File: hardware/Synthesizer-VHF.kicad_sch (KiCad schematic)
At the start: 106 parts, among them J1 Screw_Terminal_01x02, J10 REF_OUT, J12 UPDI, J2 Scope, J4 USB-C 2.0 16P, J5 REF_IN, J6 Scope, J7 RFOUTA, J9 RFOUTB, U1 LM7805A, U11 SN74LVC1GU04DBVR, U2 FT231XQ, U3 ATtiny1616-M, U4 ADF4351, U5 USBLC6-2SC6, U6 LP5907MFX-3.3, U8 LP5907MFX-3.3, X1 IQXT-220-2 10MHz

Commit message: diecast-2x2: ADF4002 locks the VCTCXO to REF_IN
Add ADF4002BCPZ (LCSC C207536). REFIN is external REF_IN through the existing attenuator, AC-coupled. RFIN is an AC-coupled VCTCXO sample. SPI CLK and DATA are shared with the ADF4351; LE is PA7 and MUXOUT is PA5. Passive loop filter is 1.5 nF, 2.2 M, 10 nF for about 20 Hz at the lowest charge-pump current. PA6 holds Vc through 100 k.

Co-authored-by: Jeffrey Millar <wa1hco@users.noreply.github.com>
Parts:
- added C55: 1.5n, Capacitor_SMD:C_0603_1608Metric, symbol Device:C
- added C56: 10n, Capacitor_SMD:C_0603_1608Metric, symbol Device:C
- added C57, C58, C60, C61: 100n, Synthesizer:Cap_0402, symbol Device:C
- added C59: 100p, Synthesizer:Cap_0402, symbol Device:C
- added R34: 2.2M, Resistor_SMD:R_0603_1608Metric, symbol Device:R_Small_US
- added R35: 5K1, Synthesizer:Res_0402, symbol Device:R_Small_US
- added R36: 100k, Synthesizer:Res_0402, symbol Device:R_Small_US
- added U12: ADF4002BCPZ, Package_DFN_QFN:QFN-20-1EP_4x4mm_P0.5mm_EP2.5x2.5mm, symbol Synthesizer:ADF4002BCPZ
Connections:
- net CLK: now also U12.12 (CLK)
- net DATA: now also U12.13 (DATA)
- net GND: now also C55.2, C56.2, C59.2, C60.2, C61.2, R35.2, U12.1 (CPGND), U12.10 (DGND), U12.2 (AGND), U12.21 (EP), U12.3 (AGND), U12.9 (DGND)
- net REF_IN: now also C58.1
- net VC: now also C56.1, R34.2, R36.2
- net VDD: now also C61.1, U12.11 (CE), U12.16 (DVDD), U12.17 (DVDD)
- net VRF: now also C60.1, U12.18 (VP), U12.6 (AVDD), U12.7 (AVDD)
- net XO: now also C57.1
- net MUX4002: now reaches U3.6 (PA5)
- net MUX4002: now also U12.15 (MUXOUT)
- net DAC_HOLD: now reaches U3.7 (PA6)
- net DAC_HOLD: now also R36.1
- net LE4002: now reaches U3.8 (PA7)
- net LE4002: now also U12.14 (LE)
- new net CP: C55.1, R34.1, U12.20 (CP)
- new net REFIN4: C58.2, U12.8 (REFIN)
- new net RFINA: C57.2, U12.5 (RFINA)
- new net RFINB: C59.1, U12.4 (RFINB)
- new net RSET: R35.1, U12.19 (RSET)
- no-connect marks 12 -> 9
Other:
- note added: "ADF4002 loop filter, about 20 Hz, 50 deg phase margin. Kvco = 10 MHz * 20 ppm / 2 V = 100 Hz/V. IQXT-220-2 pulling is +/-10 to +/-15 ppm over Vc = 1.5 V +/- 1 V, so Kv is about 100-150 Hz/V. Designed at 100 Hz/V. PFD = 10 kHz with R = N = 1000 (10 MHz / 10 kHz). Lowest CP current: CPI=000, RSET=5.1k, Icp=0.625 mA. T1=(sec phi - tan phi)/wc = 2.90 ms, T2=1/(wc^2*T1)=21.9 ms. C1=1.5 nF C0G (CP to G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"

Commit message: diecast-2x2: merge scope headers into one 1x5
Replace J2 and J6 with a single 1x5 header: LD, MUX, DBG1, DBG2, GND (LCSC C124379). DBG1 and DBG2 are header pads only, because PB4 and PB5 are reserved for the lock LEDs.

Co-authored-by: Jeffrey Millar <wa1hco@users.noreply.github.com>
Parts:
- removed J2, J6: Scope, Connector_PinHeader_2.54mm:PinHeader_1x03_P2.54mm_Vertical, symbol Connector:Conn_01x03_Pin
- added J2: Scope, Connector_PinHeader_2.54mm:PinHeader_1x05_P2.54mm_Vertical, symbol Synthesizer:Conn_01x05_Pin
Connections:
- net GND: now also J2.5 (Pin_5)
- net LD: now also J2.1 (Pin_1); no longer U4.25 (LD)
- net MUX: now also J2.2 (Pin_2); no longer U4.30 (MUXOUT)
- new net DBG1: J2.3 (Pin_3)
- new net DBG2: J2.4 (Pin_4)
- no-connect marks 9 -> 11

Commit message: diecast-2x2: four reverse-mount status LEDs
Replace the 0402 status LEDs with Kingbright KPTL-3216 reverse-mount parts that shine through the board. PWR and COMM are green C598390; REF LOCK (PB4) and SYNTH LOCK (PB5) are red C598393. COMM is FT231X CBUS2, to be programmed as TX&RXLED#.

Co-authored-by: Jeffrey Millar <wa1hco@users.noreply.github.com>
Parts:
- removed D4, D5: Yellow, LED_SMD:LED_0402_1005Metric, symbol Device:LED
- removed D7: PA2, LED_SMD:LED_0402_1005Metric, symbol Device:LED
- removed D8: PA3, LED_SMD:LED_0402_1005Metric, symbol Device:LED
- removed R10, R17, R19, R8: 1K, Synthesizer:Res_0402, symbol Device:R_US
- added D11: PWR, Synthesizer:LED_KPTL-3216_ReverseMount, symbol Device:LED
- added D12: REF LOCK, Synthesizer:LED_KPTL-3216_ReverseMount, symbol Device:LED
- added D13: SYNTH LOCK, Synthesizer:LED_KPTL-3216_ReverseMount, symbol Device:LED
- added D14: COMM, Synthesizer:LED_KPTL-3216_ReverseMount, symbol Device:LED
- added R37, R38, R39, R40: 1k, Synthesizer:Res_0402, symbol Device:R_Small_US
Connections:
- net GND: now also D11.1 (K), D12.1 (K), D13.1 (K)
- net VDD: now also D14.2 (A), R37.1
- net REF_LOCK: now reaches U3.10 (PB4)
- net REF_LOCK: now also R38.1
- net SYNTH_LOCK: now reaches U3.9 (PB5)
- net SYNTH_LOCK: now also R39.1
- net RXLED/: no longer names the net of U2.14 (CBUS1)
- net TXLED/ renamed CBUS_ACT
- net CBUS_ACT: now also R40.2
- new net COMM_K: D14.1 (K), R40.1
- new net PWR_A: D11.2 (A), R37.2
- new net REFLED: D12.2 (A), R38.2
- new net SYNLED: D13.2 (A), R39.2
- no-connect marks 11 -> 12
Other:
- note added: "CBUS2 (pin 7) is the COMM LED, active low. Program it as TX&RXLED#."
- note added: "PCB: 1.5 mm hole under each LED with GND via ring (waveguide below cutoff). Reverse-mount Kingbright KPTL-3216. Light exits the bottom face. PWR and COMM are green KPTL-3216CGCK-01 (C598390). REF LOCK and SYNTH LOCK are red KPTL-3216SURCK-01 (C598393). Blue KPTL-3216QBC-D-01 is on LCSC but Vf is 3.3 V, so it is not used on this 3.3 V rail."
- note removed: "CBUS signals use defaults"

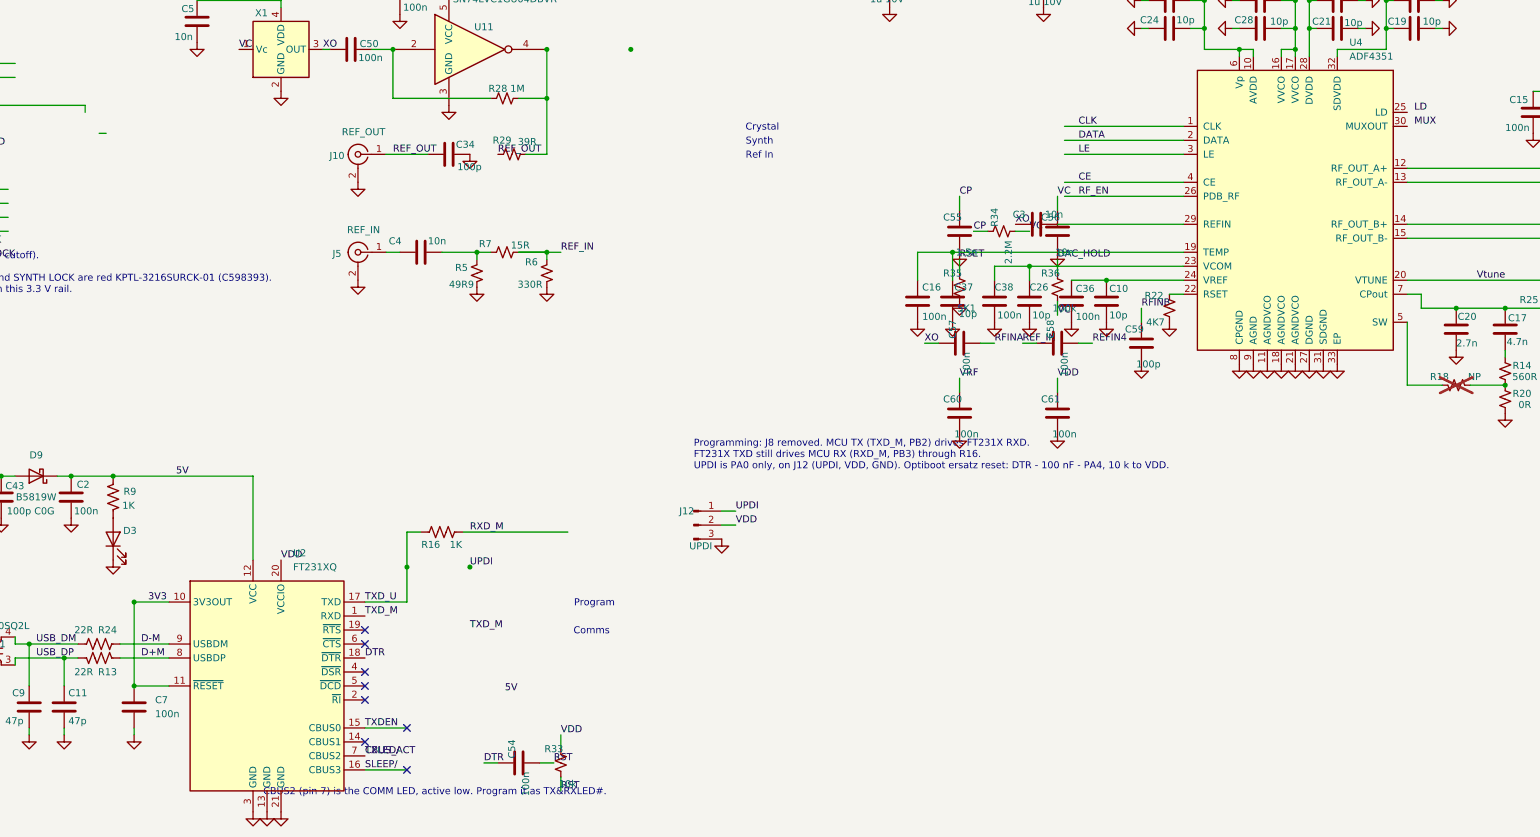
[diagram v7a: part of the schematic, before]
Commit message: diecast-2x2: make the schematic load in KiCad 10 ERC
Escape multiline notes, fix symbol property hide flags, drop dangling labels left by the removed headers, and put LD and MUX back on the ADF4351 pins.

Co-authored-by: Jeffrey Millar <wa1hco@users.noreply.github.com>
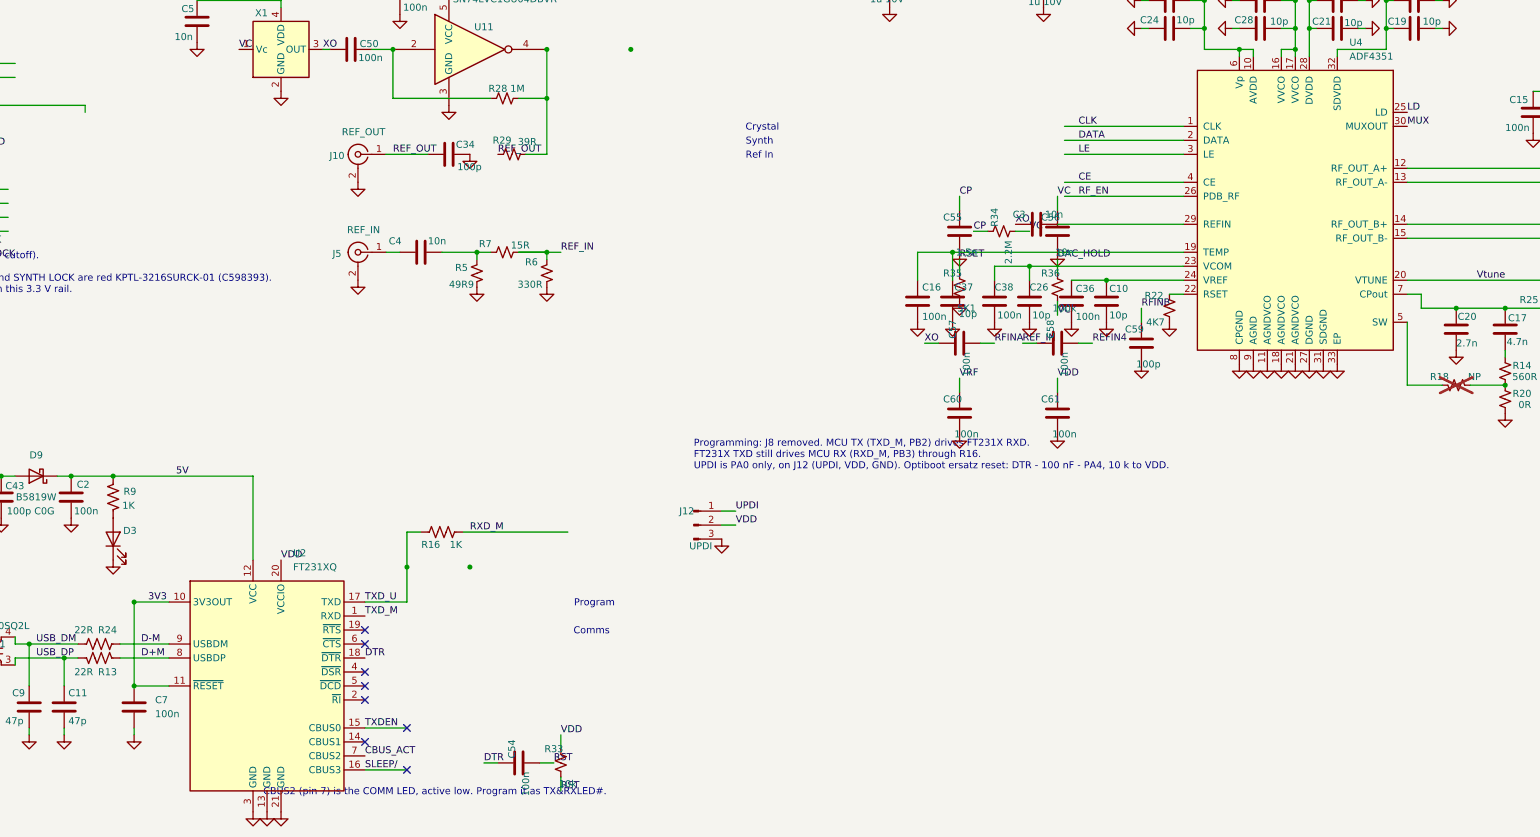
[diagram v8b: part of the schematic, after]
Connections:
- net LD: now also U4.25 (LD)
- net MUX: now also U4.30 (MUXOUT)
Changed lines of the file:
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@@
 		)
 	)
-	(wire
-		(pts
-			(xy 93.98 139.7) (xy 92.71 139.7)
-		)
-		(stroke
-			(width 0)
-			(type default)
-		)
-	)
-	(wire
+		(wire
 		(pts
 			(xy 374.65 139.7) (xy 374.65 156.21)
@@
 		)
 	)
-	(label "TXD_M"
-		(at 160.02 229.87 0)
-		(effects
-			(font
-				(size 1.27 1.27)
-			)
-			(justify left bottom)
-		)
-	)
-	(label "LD"
-		(at 331.47 135.89 0)
-		(effects
-			(font
-				(size 1.27 1.27)
-			)
-			(justify left bottom)
-		)
-	)
-	(label "5V_USB"
+			(label "5V_USB"
 		(at 67.31 201.93 0)
 		(effects
@@
 		)
 	)
-	(label "5V"
-		(at 166.37 241.3 0)
-		(effects
-			(font
-				(size 1.27 1.27)
-			)
-			(justify left bottom)
-		)
-	)
-	(label "RF_EN"
+		(label "RF_EN"
 		(at 270.51 151.13 0)
 		(effects
@@
 		)
 	)
-	(label "UPDI"
-		(at 160.02 218.44 0)
-		(effects
-			(font
-				(size 1.27 1.27)
-			)
-			(justify left bottom)
-		)
-	)
-	(label "TXLED{slash}"
-		(at 140.97 252.73 0)
-		(effects
-			(font
-				(size 1.27 1.27)
-			)
-			(justify left bottom)
-		)
-	)
-	(label "5V"
+			(label "5V"
 		(at 106.68 201.93 0)
 		(effects
@@
 		)
 	)
-	(label "MUX"
-		(at 331.47 138.43 0)
-		(effects
-			(font
-				(size 1.27 1.27)
-			)
-			(justify left bottom)
-		)
-	)
-	(symbol
+		(symbol
 		(lib_id "Device:C")
 		(at 236.22 43.18 0)
@@
 		)
 	)
-	(text "Digital 3.3 V (VDD): ATtiny, FT231X VCCIO, ADF4002 DVDD, VCTCXO, REF buffer.
-Fed from the VRF LP5907 through FB2. VVCO is its own LP5907. ADF4351 AVDD/Vp are on VRF."
+	(text "Digital 3.3 V (VDD): ATtiny, FT231X VCCIO, ADF4002 DVDD, VCTCXO, REF buffer.\nFed from the VRF LP5907 through FB2. VVCO is its own LP5907. ADF4351 AVDD/Vp are on VRF."
 		(exclude_from_sim no)
 		(at 292.1 22.86 0)
@@
 		)
 	)
-	(text "Programming: J8 removed. MCU TX (TXD_M, PB2) drives FT231X RXD.
-FT231X TXD still drives MCU RX (RXD_M, PB3) through R16.
-UPDI is PA0 only, on J12 (UPDI, VDD, GND). Optiboot ersatz reset: DTR - 100 nF - PA4, 10 k to VDD."
+	(text "Programming: J8 removed. MCU TX (TXD_M, PB2) drives FT231X RXD.\nFT231X TXD still drives MCU RX (RXD_M, PB3) through R16.\nUPDI is PA0 only, on J12 (UPDI, VDD, GND). Optiboot ersatz reset: DTR - 100 nF - PA4, 10 k to VDD."
 		(exclude_from_sim no)
 		(at 200.66 198.12 0)
@@
 		)
 	)
-	(text "REF_OUT: after U11, 39 ohm series and 100 pF to GND. RC edge softener, not a sine filter.
-VCTCXO output (XO) is AC-coupled to ADF4351 REFIN (C3), and to U11."
+	(text "REF_OUT: after U11, 39 ohm series and 100 pF to GND. RC edge softener, not a sine filter.\nVCTCXO output (XO) is AC-coupled to ADF4351 REFIN (C3), and to U11."
 		(exclude_from_sim no)
 		(at 125.73 100.33 0)
@@
 		)
 	)
-	(text "ADF4002 loop filter, about 20 Hz, 50 deg phase margin.
-Kvco = 10 MHz * 20 ppm / 2 V = 100 Hz/V.
-IQXT-220-2 pulling is +/-10 to +/-15 ppm over Vc = 1.5 V +/- 1 V, so Kv is about 100-150 Hz/V. Designed at 100 Hz/V.
-PFD = 10 kHz with R = N = 1000 (10 MHz / 10 kHz). Lowest CP current: CPI=000, RSET=5.1k, Icp=0.625 mA.
-T1=(sec phi - tan phi)/wc = 2.90 ms, T2=1/(wc^2*T1)=21.9 ms.
-C1=1.5 nF C0G (CP to GND), R=2.2 M, C2=10 nF C0G (Vc to GND).
-Free-run hold: ATtiny DAC PA6 through 100 k to Vc. Tri-state the charge pump to hold; while locking, Icp overrides the 100 k.
-ADF4002 REFIN is external /REF_IN (J5, existing attenuator, AC coupled). RFIN is the VCTCXO sample.
-SPI CLK/DATA shared with the ADF4351. LE is PA7. MUXOUT (digital lock detect) is PA5.
-REFIN below 20 MHz needs slew > 50 V/us (ADF4002 datasheet). A 10 MHz sine should be squared or > about 1.6 Vpp."
+	(text "ADF4002 loop filter, about 20 Hz, 50 deg phase margin.\nKvco = 10 MHz * 20 ppm / 2 V = 100 Hz/V.\nIQXT-220-2 pulling is +/-10 to +/-15 ppm over Vc = 1.5 V +/- 1 V, so Kv is about 100-150 Hz/V. Designed at 100 Hz/V.\nPFD = 10 kHz with R = N = 1000 (10 MHz / 10 kHz). Lowest CP current: CPI=000, RSET=5.1k, Icp=0.625 mA.\nT1=(sec phi - tan phi)/wc = 2.90 ms, T2=1/(wc^2*T1)=21.9 ms.\nC1=1.5 nF C0G (CP to GND), R=2.2 M, C2=10 nF C0G (Vc to GND).\nFree-run hold: ATtiny DAC PA6 through 100 k to Vc. Tri-state the charge pump to hold; while locking, Icp overrides the 100 k.\nADF4002 REFIN is external /REF_IN (J5, existing attenuator, AC coupled). RFIN is the VCTCXO sample.\nSPI CLK/DATA shared with the ADF4351. LE is PA7. MUXOUT (digital lock detect) is PA5.\nREFIN below 20 MHz needs slew > 50 V/us (ADF4002 datasheet). A 10 MHz sine should be squared or > about 1.6 Vpp."
 		(exclude_from_sim no)
 		(at 330.2 25.4 0)
@@
 		)
 	)
-	(text "PCB: 1.5 mm hole under each LED with GND via ring (waveguide below cutoff).
-Reverse-mount Kingbright KPTL-3216. Light exits the bottom face.
-PWR and COMM are green KPTL-3216CGCK-01 (C598390). REF LOCK and SYNTH LOCK are red KPTL-3216SURCK-01 (C598393).
-Blue KPTL-3216QBC-D-01 is on LCSC but Vf is 3.3 V, so it is not used on this 3.3 V rail."
+	(text "PCB: 1.5 mm hole under each LED with GND via ring (waveguide below cutoff).\nReverse-mount Kingbright KPTL-3216. Light exits the bottom face.\nPWR and COMM are green KPTL-3216CGCK-01 (C598390). REF LOCK and SYNTH LOCK are red KPTL-3216SURCK-01 (C598393).\nBlue KPTL-3216QBC-D-01 is on LCSC but Vf is 3.3 V, so it is not used on this 3.3 V rail."
 		(exclude_from_sim no)
 		(at 12.7 165.1 0)
@@
 		(at 140.97 250.19)
 	)
+	(label "LD"
+		(at 330.2 135.89 0)
+		(effects
+			(font
+				(size 1.27 1.27)
+			)
+			(justify left bottom)
+		)
+	)
+	(label "MUX"
+		(at 330.2 138.43 0)
+		(effects
+			(font
+				(size 1.27 1.27)
+			)
+			(justify left bottom)
+		)
+	)
 	(sheet_instances
